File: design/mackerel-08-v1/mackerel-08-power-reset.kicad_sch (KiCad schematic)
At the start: 31 parts, among them J2 DC_Jack, SW1 SW_Push, SW2 SW_SPDT, U15 NE555P

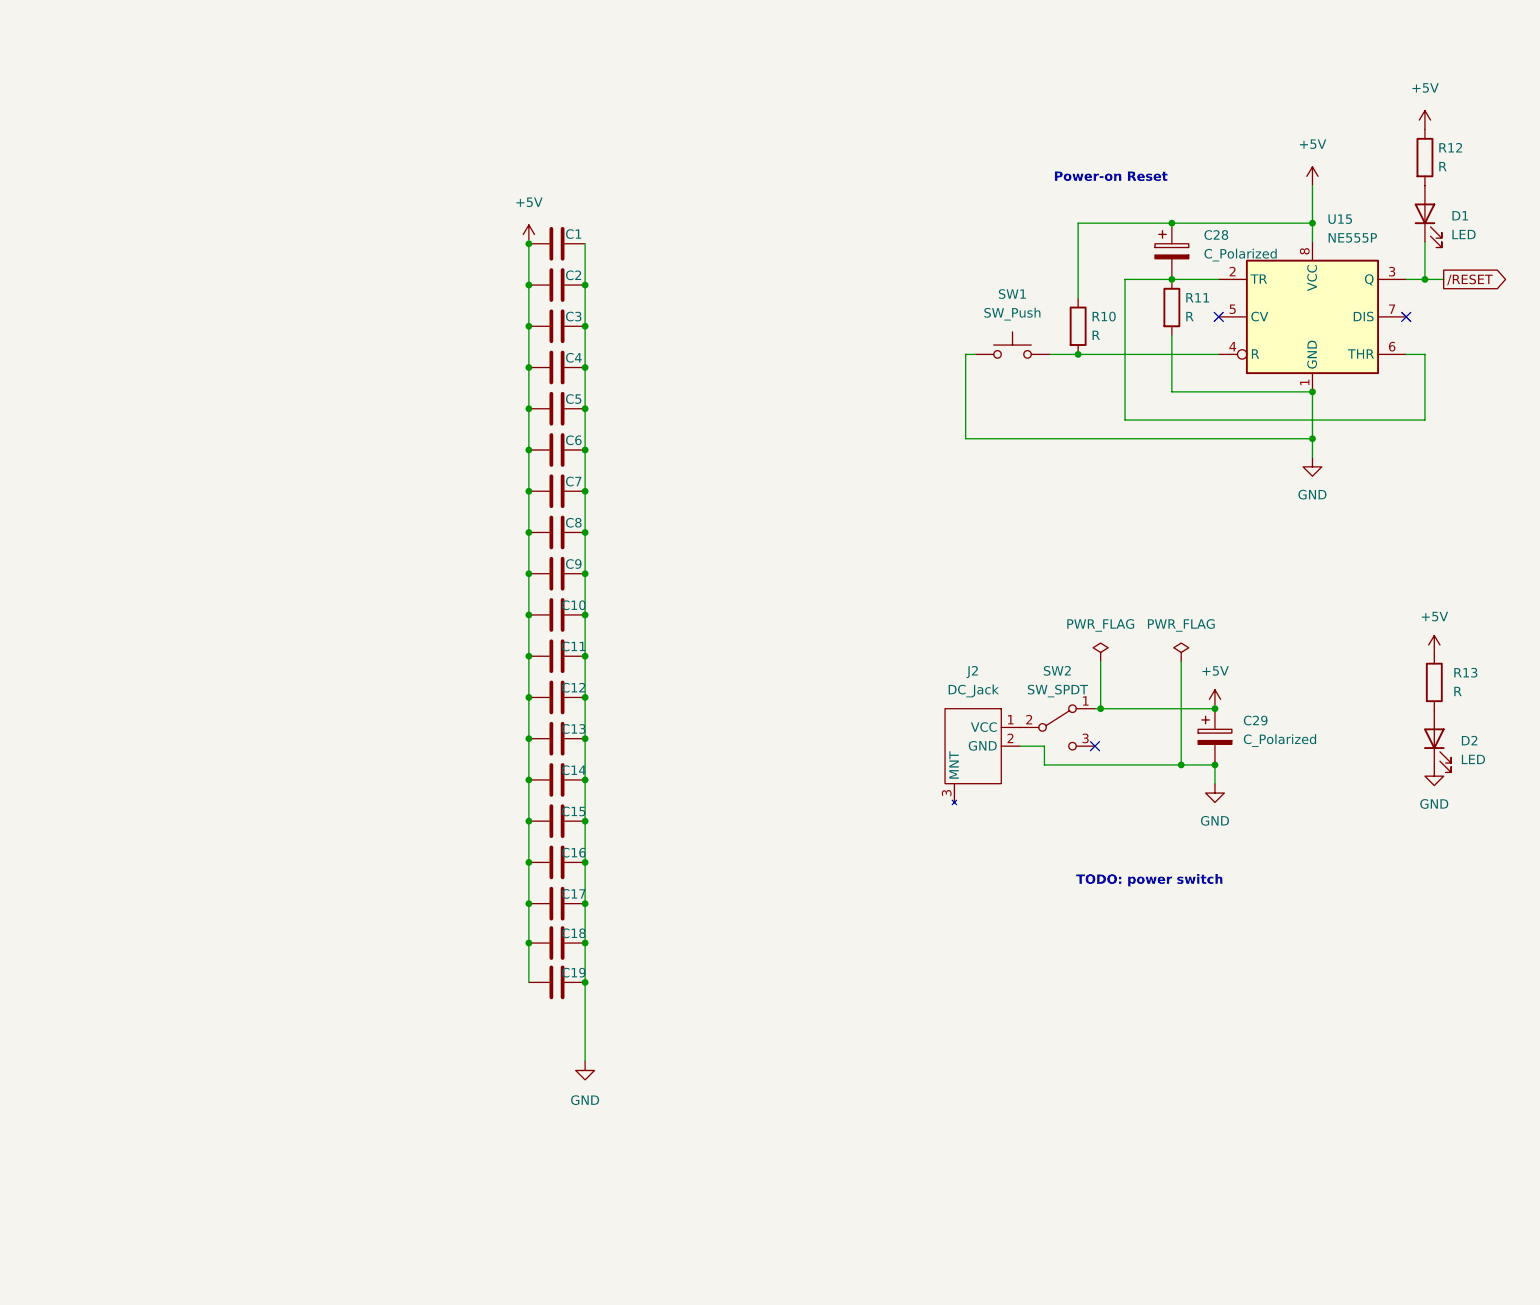
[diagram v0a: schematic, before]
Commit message: Clean up the schematic, ready for final routing
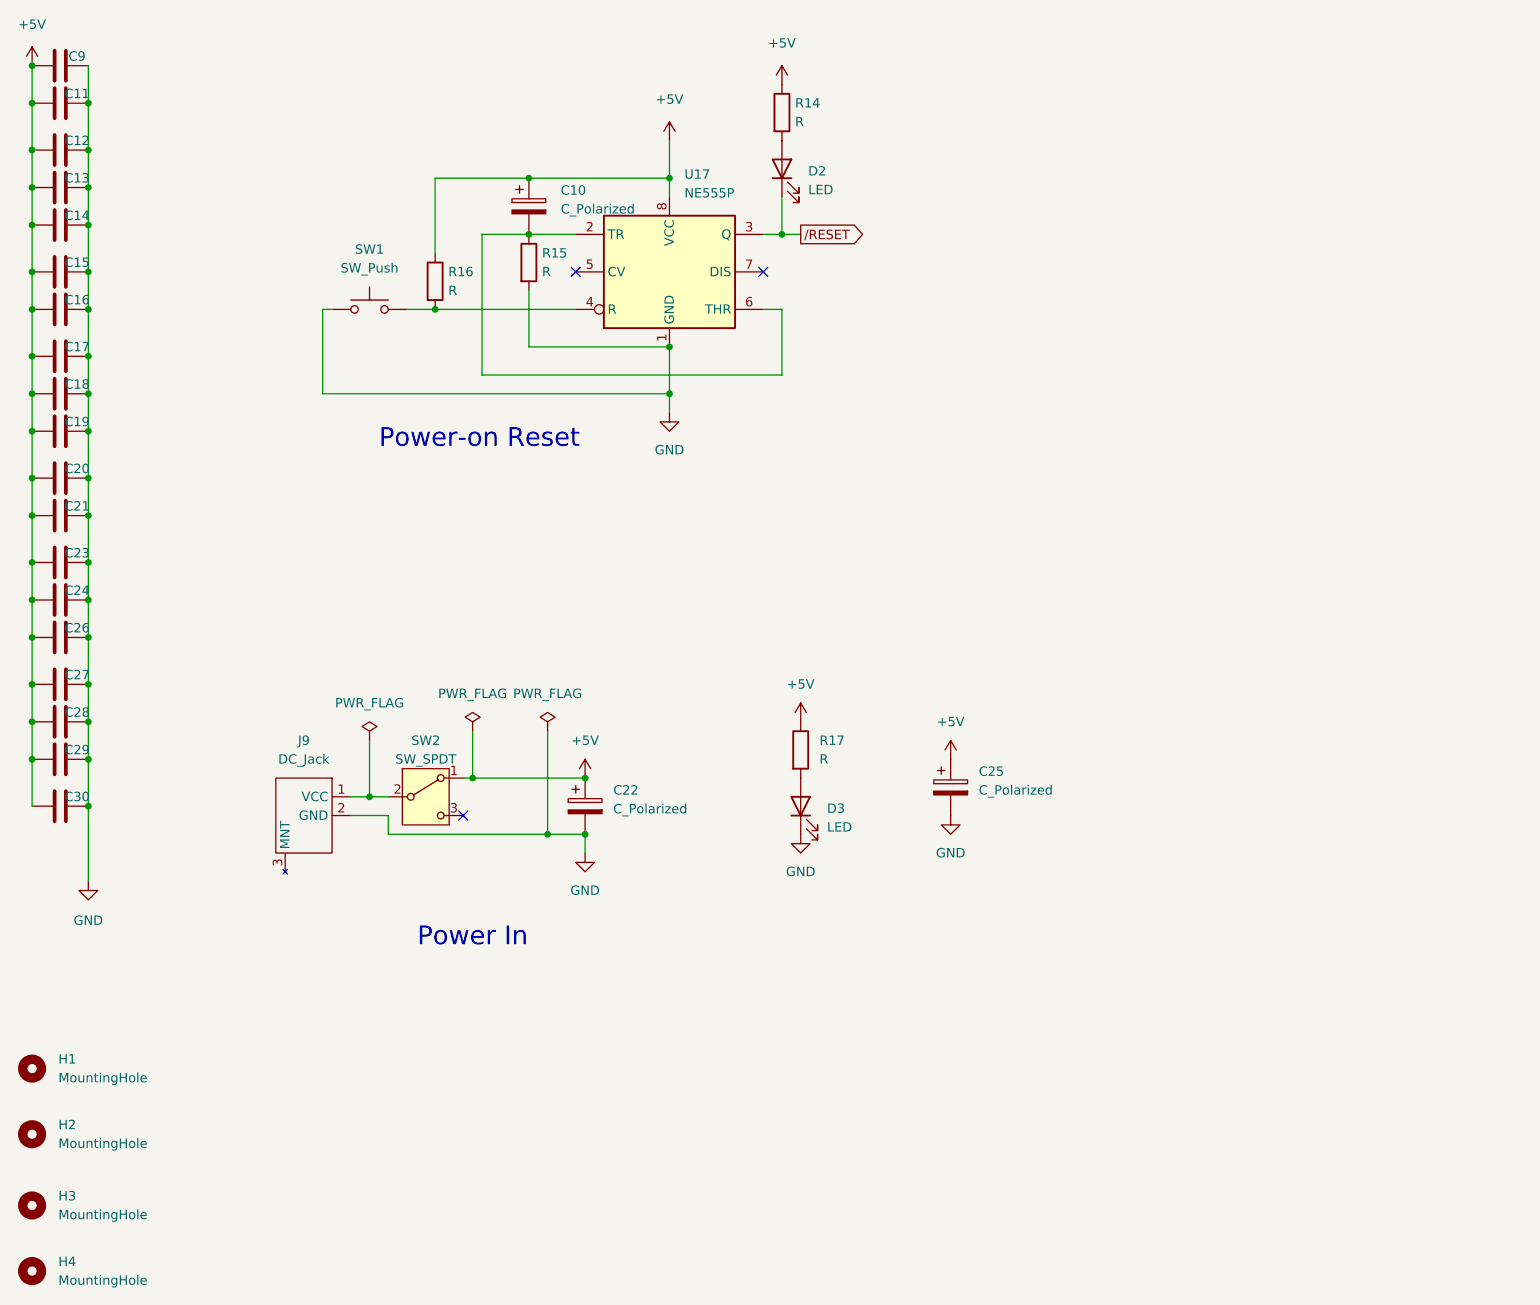
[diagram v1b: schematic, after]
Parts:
- added C25: C_Polarized, Capacitor_THT:CP_Radial_D10.0mm_P5.00mm, symbol Device:C_Polarized
- added H1, H2, H3, H4: MountingHole, MountingHole:MountingHole_3.2mm_M3_Pad, symbol Mechanical:MountingHole
- renumbered C28 to C10, C2 to C11, C3 to C12, C4 to C13, C5 to C14, C6 to C15, C7 to C16, C8 to C17, C9 to C18, C10 to C19, C11 to C20, C12 to C21, C29 to C22, C13 to C23, C14 to C24, C15 to C26, C16 to C27, C17 to C28, C18 to C29, C19 to C30, C1 to C9, D1 to D2, D2 to D3, J2 to J9, R12 to R14, R11 to R15, R10 to R16, R13 to R17, U15 to U17
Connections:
- net +5V: now also C25.1
- net GND: now also C25.2
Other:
- note added: "Power In"
- note removed: "TODO: power switch"
- company: (none) -> Colin Maykish
- title: (none) -> Mackerel-08 SBC v1
- moved on the sheet: C10, C11, C12, C13, C14, C15, C16, C17, C18, C19, C20, C21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

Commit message: Mackerel-08 v1 is fully routed, needs graphics, labels, and cleanup
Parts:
- removed C30, C9: C, Capacitor_THT:C_Disc_D4.3mm_W1.9mm_P5.00mm, symbol Device:C
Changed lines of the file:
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@@
-	)
-	(junction
-		(at 30.48 125.73)
-		(diameter 0)
-		(color 0 0 0 0)
 	)
 	(junction
@@
 	)
 	(junction
-		(at 30.48 30.48)
-		(diameter 0)
-		(color 0 0 0 0)
-	)
-	(junction
 		(at 22.86 69.85)
-		(diameter 0)
-		(color 0 0 0 0)
-	)
-	(junction
-		(at 22.86 119.38)
 		(diameter 0)
 		(color 0 0 0 0)
@@
 		(color 0 0 0 0)
 	)
-	(junction
-		(at 22.86 25.4)
-		(diameter 0)
-		(color 0 0 0 0)
-	)
 	(no_connect
 		(at 96.52 53.34)
@@
 	(wire
 		(pts
-			(xy 30.48 25.4) (xy 30.48 30.48)
-		)
-		(stroke
-			(width 0)
-			(type default)
-		)
-	)
-	(wire
-		(pts
-			(xy 30.48 125.73) (xy 30.48 119.38)
+			(xy 30.48 119.38) (xy 30.48 125.73)
 		)
 		(stroke
@@
 	(wire
 		(pts
-			(xy 22.86 119.38) (xy 22.86 125.73)
-		)
-		(stroke
-			(width 0)
-			(type default)
-		)
-	)
-	(wire
-		(pts
 			(xy 71.12 127) (xy 71.12 129.54)
 		)
@@
 		(pts
 			(xy 22.86 58.42) (xy 22.86 64.77)
-		)
-		(stroke
-			(width 0)
-			(type default)
-		)
-	)
-	(wire
-		(pts
-			(xy 30.48 135.89) (xy 30.48 125.73)
 		)
 		(stroke
@@
 	(symbol
 		(lib_id "power:GND")
-		(at 30.48 135.89 0)
+		(at 30.48 125.73 0)
 		(unit 1)
 		(exclude_from_sim no)
@@
 		(fields_autoplaced yes)
 		(property "Reference" "#PWR073"
-			(at 30.48 142.24 0)
+			(at 30.48 132.08 0)
 			(effects
 				(font
@@
 		)
 		(property "Value" "GND"
-			(at 30.48 141.224 0)
+			(at 30.48 131.064 0)
 			(effects
 				(font
@@
 		)
 		(property "Footprint" ""
-			(at 30.48 135.89 0)
+			(at 30.48 125.73 0)
 			(effects
 				(font
@@
 		)
 		(property "Datasheet" ""
-			(at 30.48 135.89 0)
+			(at 30.48 125.73 0)
 			(effects
 				(font
@@
 		)
 		(property "Description" "Power symbol creates a global label with name \"GND\" , ground"
-			(at 30.48 135.89 0)
+			(at 30.48 125.73 0)
 			(effects
 				(font
@@
 	(symbol
 		(lib_id "Device:C")
-		(at 26.67 25.4 90)
-		(unit 1)
-		(exclude_from_sim no)
-		(in_bom yes)
-		(on_board yes)
-		(dnp no)
-		(property "Reference" "C9"
-			(at 28.956 24.13 90)
-			(effects
-				(font
-					(size 1.27 1.27)
-				)
-			)
-		)
-		(property "Value" "C"
-			(at 26.67 21.082 90)
-			(effects
-				(font
-					(size 1.27 1.27)
-				)
-				(hide yes)
-			)
-		)
-		(property "Footprint" "Capacitor_THT:C_Disc_D4.3mm_W1.9mm_P5.00mm"
-			(at 30.48 24.4348 0)
-			(effects
-				(font
-					(size 1.27 1.27)
-				)
-				(hide yes)
-			)
-		)
-		(property "Datasheet" "~"
-			(at 26.67 25.4 0)
-			(effects
-				(font
-					(size 1.27 1.27)
-				)
-				(hide yes)
-			)
-		)
-		(property "Description" "Unpolarized capacitor"
-			(at 26.67 25.4 0)
-			(effects
-				(font
-					(size 1.27 1.27)
-				)
-				(hide yes)
-			)
-		)
-		(pin "1"
-		)
-		(pin "2"
-		)
-		(instances
-			(project "mackerel-08-v1"
-				(path "/d8b1bce0-db11-4fa6-8e54-fcae9a8fcfc2/7a389a7c-8317-4082-87da-094545447ed4"
-					(reference "C9")
-					(unit 1)
-				)
-			)
-		)
-	)
-	(symbol
-		(lib_id "Device:C")
 		(at 26.67 81.28 90)
 		(unit 1)
@@
 					(unit 1)
 				)
-			)
-		)
-	)
-	(symbol
-		(lib_id "Device:C")
-		(at 26.67 125.73 90)
-		(unit 1)
-		(exclude_from_sim no)
-		(in_bom yes)
-		(on_board yes)
-		(dnp no)
-		(property "Reference" "C30"
-			(at 28.956 124.46 90)
-			(effects
-				(font
-					(size 1.27 1.27)
-				)
-			)
-		)
-		(property "Value" "C"
-			(at 26.67 121.412 90)
-			(effects
-				(font
-					(size 1.27 1.27)
-				)
-				(hide yes)
-			)
-		)
-		(property "Footprint" "Capacitor_THT:C_Disc_D4.3mm_W1.9mm_P5.00mm"
-			(at 30.48 124.7648 0)
-			(effects
-				(font
-					(size 1.27 1.27)
-				)
-				(hide yes)
-			)
-		)
-		(property "Datasheet" "~"
-			(at 26.67 125.73 0)
-			(effects
-				(font
-					(size 1.27 1.27)
-				)
-				(hide yes)
-			)
-		)
-		(property "Description" "Unpolarized capacitor"
-			(at 26.67 125.73 0)
-			(effects
-				(font
-					(size 1.27 1.27)
-				)
-				(hide yes)
-			)
-		)
-		(pin "1"
-		)
-		(pin "2"
-		)
-		(instances
-			(project "mackerel-08-v1"
-				(path "/d8b1bce0-db11-4fa6-8e54-fcae9a8fcfc2/7a389a7c-8317-4082-87da-094545447ed4"
-					(reference "C30")
-					(unit 1)
-				)
